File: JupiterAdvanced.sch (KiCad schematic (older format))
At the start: 217 parts, among them SW1 SW_Push, U1 PRTR5V0U2X, U2 AT90USB1286-AU, Y1 16MHz

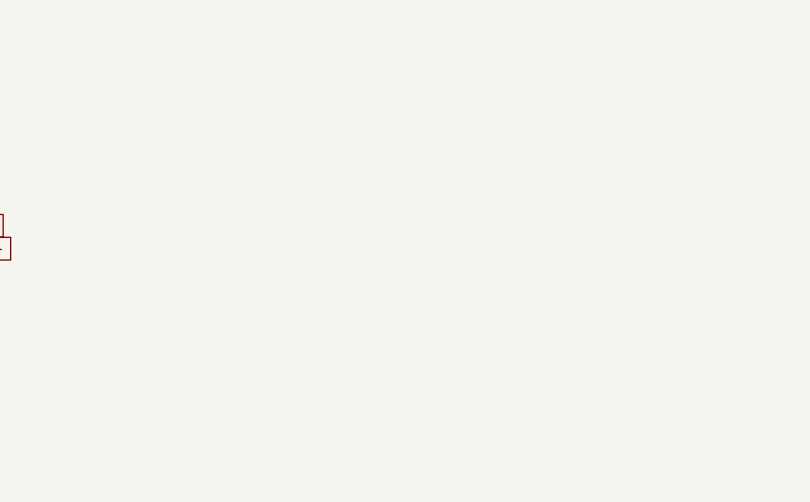
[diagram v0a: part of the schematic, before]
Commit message: Gerber Files updated, Drill holes added
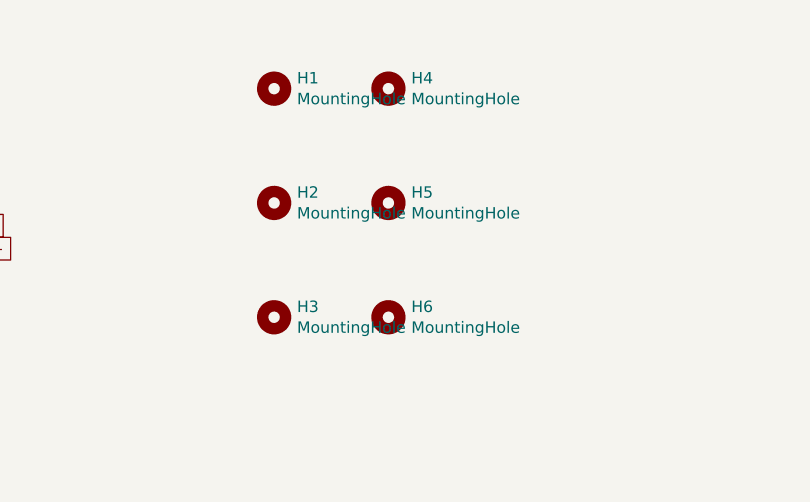
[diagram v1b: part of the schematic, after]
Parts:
- added H1, H2, H3, H4, H5, H6: MountingHole, MountingHole:MountingHole_2.5mm, symbol Mechanical:MountingHole
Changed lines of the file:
@@
 NoConn ~ 11050 4250
 NoConn ~ 11050 2350
+$Comp
+L Mechanical:MountingHole H4
+U 1 1 607B1DF0
+P 5900 1000
+F 0 "H4" H 6000 1046 50  0000 L CNN
+F 1 "MountingHole" H 6000 955 50  0000 L CNN
+F 2 "MountingHole:MountingHole_2.5mm" H 5900 1000 50  0001 C CNN
+F 3 "~" H 5900 1000 50  0001 C CNN
+	1    5900 1000
+	1    0    0    -1
+$EndComp
+$Comp
+L Mechanical:MountingHole H5
+U 1 1 607B3E5A
+P 5900 1500
+F 0 "H5" H 6000 1546 50  0000 L CNN
+F 1 "MountingHole" H 6000 1455 50  0000 L CNN
+F 2 "MountingHole:MountingHole_2.5mm" H 5900 1500 50  0001 C CNN
+F 3 "~" H 5900 1500 50  0001 C CNN
+	1    5900 1500
+	1    0    0    -1
+$EndComp
+$Comp
+L Mechanical:MountingHole H6
+U 1 1 607B462B
+P 5900 2000
+F 0 "H6" H 6000 2046 50  0000 L CNN
+F 1 "MountingHole" H 6000 1955 50  0000 L CNN
+F 2 "MountingHole:MountingHole_2.5mm" H 5900 2000 50  0001 C CNN
+F 3 "~" H 5900 2000 50  0001 C CNN
+	1    5900 2000
+	1    0    0    -1
+$EndComp
+$Comp
+L Mechanical:MountingHole H1
+U 1 1 607B5D34
+P 5400 1000
+F 0 "H1" H 5500 1046 50  0000 L CNN
+F 1 "MountingHole" H 5500 955 50  0000 L CNN
+F 2 "MountingHole:MountingHole_2.5mm" H 5400 1000 50  0001 C CNN
+F 3 "~" H 5400 1000 50  0001 C CNN
+	1    5400 1000
+	1    0    0    -1
+$EndComp
+$Comp
+L Mechanical:MountingHole H2
+U 1 1 607B60CD
+P 5400 1500
+F 0 "H2" H 5500 1546 50  0000 L CNN
+F 1 "MountingHole" H 5500 1455 50  0000 L CNN
+F 2 "MountingHole:MountingHole_2.5mm" H 5400 1500 50  0001 C CNN
+F 3 "~" H 5400 1500 50  0001 C CNN
+	1    5400 1500
+	1    0    0    -1
+$EndComp
+$Comp
+L Mechanical:MountingHole H3
+U 1 1 607B643D
+P 5400 2000
+F 0 "H3" H 5500 2046 50  0000 L CNN
+F 1 "MountingHole" H 5500 1955 50  0000 L CNN
+F 2 "MountingHole:MountingHole_2.5mm" H 5400 2000 50  0001 C CNN
+F 3 "~" H 5400 2000 50  0001 C CNN
+	1    5400 2000
+	1    0    0    -1
+$EndComp
 $EndSCHEMATC

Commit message: LCSC added to USB system
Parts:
- F11: LCSC (none) -> C163133
- R1, R3: LCSC (none) -> C27834
- U1: LCSC (none) -> C558444
- USB1: LCSC (none) -> C165948
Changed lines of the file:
@@
 F 2 "Type-C:HRO-TYPE-C-31-M-12-Assembly" H 1350 1550 60  0001 C CNN
 F 3 "" H 1350 1550 60  0001 C CNN
+F 4 "C165948" H 1350 1550 50  0001 C CNN "LCSC"
 	1    1350 1550
 	1    0    0    -1
@@
 F 2 "Fuse:Fuse_1206_3216Metric" H 2600 900 50  0001 L CNN
 F 3 "~" H 2550 1100 50  0001 C CNN
+F 4 "C163133" V 2550 1100 50  0001 C CNN "LCSC"
 	1    2550 1100
 	0    1    1    0
@@
 F 2 "Resistor_SMD:R_0805_2012Metric" H 2050 2350 50  0001 C CNN
 F 3 "~" H 2050 2350 50  0001 C CNN
+F 4 "C27834" H 2050 2350 50  0001 C CNN "LCSC"
 	1    2050 2350
 	1    0    0    -1
@@
 F 2 "Resistor_SMD:R_0805_2012Metric" H 2400 2350 50  0001 C CNN
 F 3 "~" H 2400 2350 50  0001 C CNN
+F 4 "C27834" H 2400 2350 50  0001 C CNN "LCSC"
 	1    2400 2350
 	1    0    0    -1
@@
 F 2 "random-keyboard-parts:SOT143B" H 3200 2400 60  0001 C CNN
 F 3 "" H 3200 2400 60  0001 C CNN
+F 4 "C558444 " H 3200 2400 50  0001 C CNN "LCSC"
 	1    3200 2400
 	-1   0    0    1

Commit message: LCSC parts numbers added
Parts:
- C1, C2, C3: LCSC (none) -> C1711
- C4: LCSC (none) -> C15850
- C5, C6: LCSC (none) -> C1804
- C7: LCSC (none) -> C28323
- R5, R6: LCSC (none) -> C17561
- R7, R8: LCSC (none) -> C17414
- Y1: LCSC (none) -> C89379
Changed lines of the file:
@@
 F 2 "Resistor_SMD:R_0805_2012Metric" H 10500 3750 50  0001 C CNN
 F 3 "~" H 10500 3750 50  0001 C CNN
+F 4 "C17414" V 10500 3750 50  0001 C CNN "LCSC"
 	1    10500 3750
 	0    1    1    0
@@
 F 2 "Capacitor_SMD:C_0805_2012Metric" H 10150 3150 50  0001 C CNN
 F 3 "~" H 10150 3150 50  0001 C CNN
+F 4 "C28323" H 10150 3150 50  0001 C CNN "LCSC"
 	1    10150 3150
 	-1   0    0    1
@@
 F 2 "Capacitor_SMD:C_0805_2012Metric" H 9400 1350 50  0001 C CNN
 F 3 "~" H 9400 1350 50  0001 C CNN
+F 4 "C1711" H 9400 1350 50  0001 C CNN "LCSC"
 	1    9400 1350
 	1    0    0    -1
@@
 F 2 "Capacitor_SMD:C_0805_2012Metric" H 9800 1350 50  0001 C CNN
 F 3 "~" H 9800 1350 50  0001 C CNN
+F 4 "C15850" H 9800 1350 50  0001 C CNN "LCSC"
 	1    9800 1350
 	1    0    0    -1
@@
 F 2 "Capacitor_SMD:C_0805_2012Metric" H 9000 1350 50  0001 C CNN
 F 3 "~" H 9000 1350 50  0001 C CNN
+F 4 "C1711" H 9000 1350 50  0001 C CNN "LCSC"
 	1    9000 1350
 	1    0    0    -1
@@
 F 2 "Capacitor_SMD:C_0805_2012Metric" H 8600 1350 50  0001 C CNN
 F 3 "~" H 8600 1350 50  0001 C CNN
+F 4 "C1711" H 8600 1350 50  0001 C CNN "LCSC"
 	1    8600 1350
 	1    0    0    -1
@@
 F 2 "Crystal:Crystal_SMD_3225-4Pin_3.2x2.5mm" H 10300 2050 50  0001 C CNN
 F 3 "~" H 10300 2050 50  0001 C CNN
+F 4 "C89379" V 10300 2050 50  0001 C CNN "LCSC"
 	1    10300 2050
 	0    1    1    0
@@
 F 2 "Capacitor_SMD:C_0805_2012Metric" H 9900 1850 50  0001 C CNN
 F 3 "~" H 9900 1850 50  0001 C CNN
+F 4 "C1804" V 9900 1850 50  0001 C CNN "LCSC"
 	1    9900 1850
 	0    1    1    0
@@
 F 2 "Capacitor_SMD:C_0805_2012Metric" H 9900 2200 50  0001 C CNN
 F 3 "~" H 9900 2200 50  0001 C CNN
+F 4 "C1804" V 9900 2200 50  0001 C CNN "LCSC"
 	1    9900 2200
 	0    1    1    0
@@
 F 2 "Resistor_SMD:R_0805_2012Metric" H 11000 1200 50  0001 C CNN
 F 3 "~" H 11000 1200 50  0001 C CNN
+F 4 "C17414" H 11000 1200 50  0001 C CNN "LCSC"
 	1    11000 1200
 	1    0    0    -1
@@
 F 2 "Resistor_SMD:R_0805_2012Metric" H 10200 2750 50  0001 C CNN
 F 3 "~" H 10200 2750 50  0001 C CNN
+F 4 "C17561" V 10200 2750 50  0001 C CNN "LCSC"
 	1    10200 2750
 	0    1    1    0
@@
 F 2 "Resistor_SMD:R_0805_2012Metric" H 10500 2850 50  0001 C CNN
 F 3 "~" H 10500 2850 50  0001 C CNN
+F 4 "C17561" V 10500 2850 50  0001 C CNN "LCSC"
 	1    10500 2850
 	0    1    1    0

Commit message: LCSC parts numbers added
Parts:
- D1, D10, D100, D11, D12, D13, D14, D15, D16, D17, D18, D19, D2, D20, D21, D22, D23, D24, D25, D26, D27, D28, D29, D3, D30, D32, D33, D34, D35, D36, D37, D38, D39, D4, D40, D41, D42, D43, D44, D45, D46, D47, D48, D49, D5, D50, D51, D52, D53, D54, D55, D56, D58, D59, D6, D60, D61, D62, D63, D64, D65, D66, D67, D68, D69, D7, D70, D71, D72, D73, D74, D75, D76, D77, D78, D79, D8, D80, D81, D82, D83, D84, D85, D86, D87, D88, D89, D9, D90, D91, D92, D93, D94, D95, D96, D97, D98, D99: LCSC (none) -> C81598
- D57: LSCS (none) -> C81598

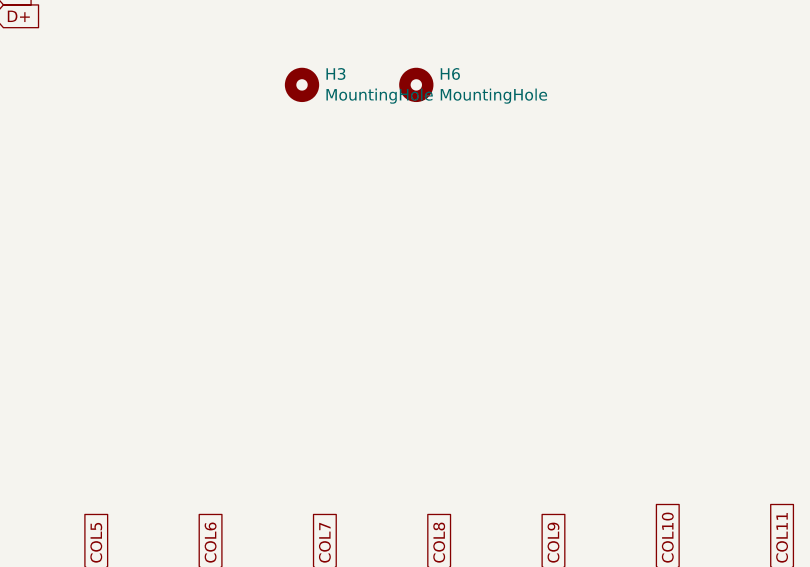
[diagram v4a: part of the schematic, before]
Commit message: Ferret Bead added on USB Ground
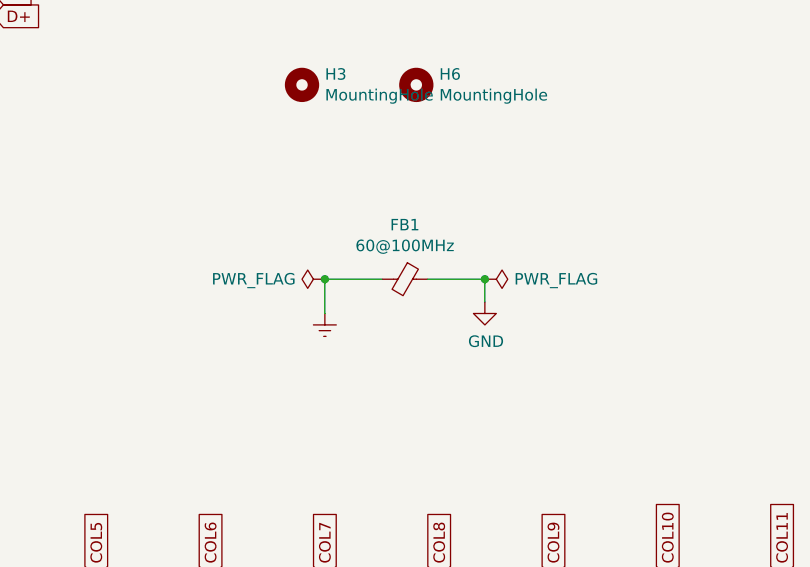
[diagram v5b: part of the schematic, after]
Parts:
- added FB1: 60@100MHz, Inductor_SMD:L_0805_2012Metric, symbol Device:Ferrite_Bead_Small
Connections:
- net labels added: Earth
- wire segments 405 -> 409
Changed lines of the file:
@@
 	1    0    0    -1
 $EndComp
+$Comp
+L Device:Ferrite_Bead_Small FB1
+U 1 1 607F6A7A
+P 5850 2850
+F 0 "FB1" V 5613 2850 50  0000 C CNN
+F 1 "60@100MHz" V 5704 2850 50  0000 C CNN
+F 2 "Inductor_SMD:L_0805_2012Metric" V 5780 2850 50  0001 C CNN
+F 3 "~" H 5850 2850 50  0001 C CNN
+	1    5850 2850
+	0    1    1    0
+$EndComp
+$Comp
+L power:GND #PWR0115
+U 1 1 607F9CFC
+P 6200 2950
+F 0 "#PWR0115" H 6200 2700 50  0001 C CNN
+F 1 "GND" H 6205 2777 50  0000 C CNN
+F 2 "" H 6200 2950 50  0001 C CNN
+F 3 "" H 6200 2950 50  0001 C CNN
+	1    6200 2950
+	1    0    0    -1
+$EndComp
+$Comp
+L power:Earth #PWR0116
+U 1 1 607FD133
+P 5500 3000
+F 0 "#PWR0116" H 5500 2750 50  0001 C CNN
+F 1 "Earth" H 5500 2850 50  0001 C CNN
+F 2 "" H 5500 3000 50  0001 C CNN
+F 3 "~" H 5500 3000 50  0001 C CNN
+	1    5500 3000
+	1    0    0    -1
+$EndComp
+Wire Wire Line
+	6200 2950 6200 2850
+Wire Wire Line
+	6200 2850 5950 2850
+Wire Wire Line
+	5750 2850 5500 2850
+Wire Wire Line
+	5500 2850 5500 3000
+$Comp
+L power:PWR_FLAG #FLG0104
+U 1 1 6086389D
+P 6200 2850
+F 0 "#FLG0104" H 6200 2925 50  0001 C CNN
+F 1 "PWR_FLAG" V 6200 2978 50  0000 L CNN
+F 2 "" H 6200 2850 50  0001 C CNN
+F 3 "~" H 6200 2850 50  0001 C CNN
+	1    6200 2850
+	0    1    1    0
+$EndComp
+Connection ~ 6200 2850
+$Comp
+L power:PWR_FLAG #FLG0105
+U 1 1 60866D1D
+P 5500 2850
+F 0 "#FLG0105" H 5500 2925 50  0001 C CNN
+F 1 "PWR_FLAG" V 5500 2977 50  0000 L CNN
+F 2 "" H 5500 2850 50  0001 C CNN
+F 3 "~" H 5500 2850 50  0001 C CNN
+	1    5500 2850
+	0    -1   -1   0
+$EndComp
+Connection ~ 5500 2850
 $EndSCHEMATC

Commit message: Mounting holes updated
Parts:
- H1, H2, H3, H4, H5, H6: footprint MountingHole:MountingHole_2.5mm -> MountingHole:MountingHole_2.5mm_Pad
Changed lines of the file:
@@
 F 0 "H4" H 6000 1046 50  0000 L CNN
 F 1 "MountingHole" H 6000 955 50  0000 L CNN
-F 2 "MountingHole:MountingHole_2.5mm" H 5900 1000 50  0001 C CNN
+F 2 "MountingHole:MountingHole_2.5mm_Pad" H 5900 1000 50  0001 C CNN
 F 3 "~" H 5900 1000 50  0001 C CNN
 	1    5900 1000
@@
 F 0 "H5" H 6000 1546 50  0000 L CNN
 F 1 "MountingHole" H 6000 1455 50  0000 L CNN
-F 2 "MountingHole:MountingHole_2.5mm" H 5900 1500 50  0001 C CNN
+F 2 "MountingHole:MountingHole_2.5mm_Pad" H 5900 1500 50  0001 C CNN
 F 3 "~" H 5900 1500 50  0001 C CNN
 	1    5900 1500
@@
 F 0 "H6" H 6000 2046 50  0000 L CNN
 F 1 "MountingHole" H 6000 1955 50  0000 L CNN
-F 2 "MountingHole:MountingHole_2.5mm" H 5900 2000 50  0001 C CNN
+F 2 "MountingHole:MountingHole_2.5mm_Pad" H 5900 2000 50  0001 C CNN
 F 3 "~" H 5900 2000 50  0001 C CNN
 	1    5900 2000
@@
 F 0 "H1" H 5500 1046 50  0000 L CNN
 F 1 "MountingHole" H 5500 955 50  0000 L CNN
-F 2 "MountingHole:MountingHole_2.5mm" H 5400 1000 50  0001 C CNN
+F 2 "MountingHole:MountingHole_2.5mm_Pad" H 5400 1000 50  0001 C CNN
 F 3 "~" H 5400 1000 50  0001 C CNN
 	1    5400 1000
@@
 F 0 "H2" H 5500 1546 50  0000 L CNN
 F 1 "MountingHole" H 5500 1455 50  0000 L CNN
-F 2 "MountingHole:MountingHole_2.5mm" H 5400 1500 50  0001 C CNN
+F 2 "MountingHole:MountingHole_2.5mm_Pad" H 5400 1500 50  0001 C CNN
 F 3 "~" H 5400 1500 50  0001 C CNN
 	1    5400 1500
@@
 F 0 "H3" H 5500 2046 50  0000 L CNN
 F 1 "MountingHole" H 5500 1955 50  0000 L CNN
-F 2 "MountingHole:MountingHole_2.5mm" H 5400 2000 50  0001 C CNN
+F 2 "MountingHole:MountingHole_2.5mm_Pad" H 5400 2000 50  0001 C CNN
 F 3 "~" H 5400 2000 50  0001 C CNN
 	1    5400 2000

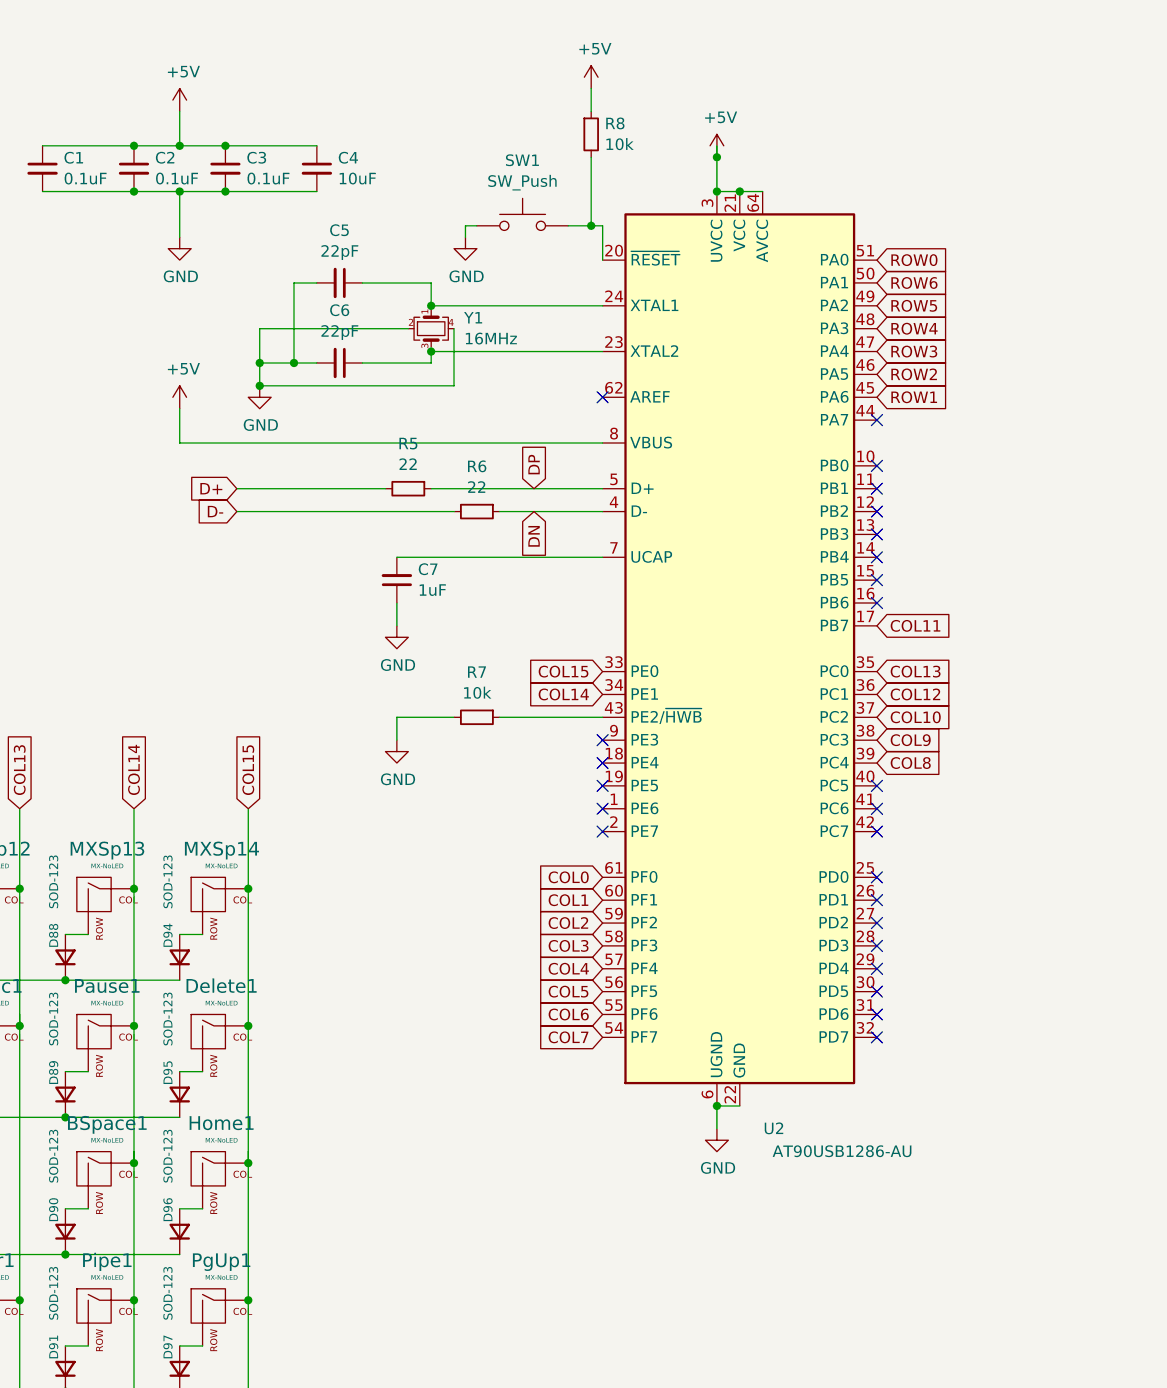
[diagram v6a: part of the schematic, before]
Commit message: ATMega32u4 MCU added
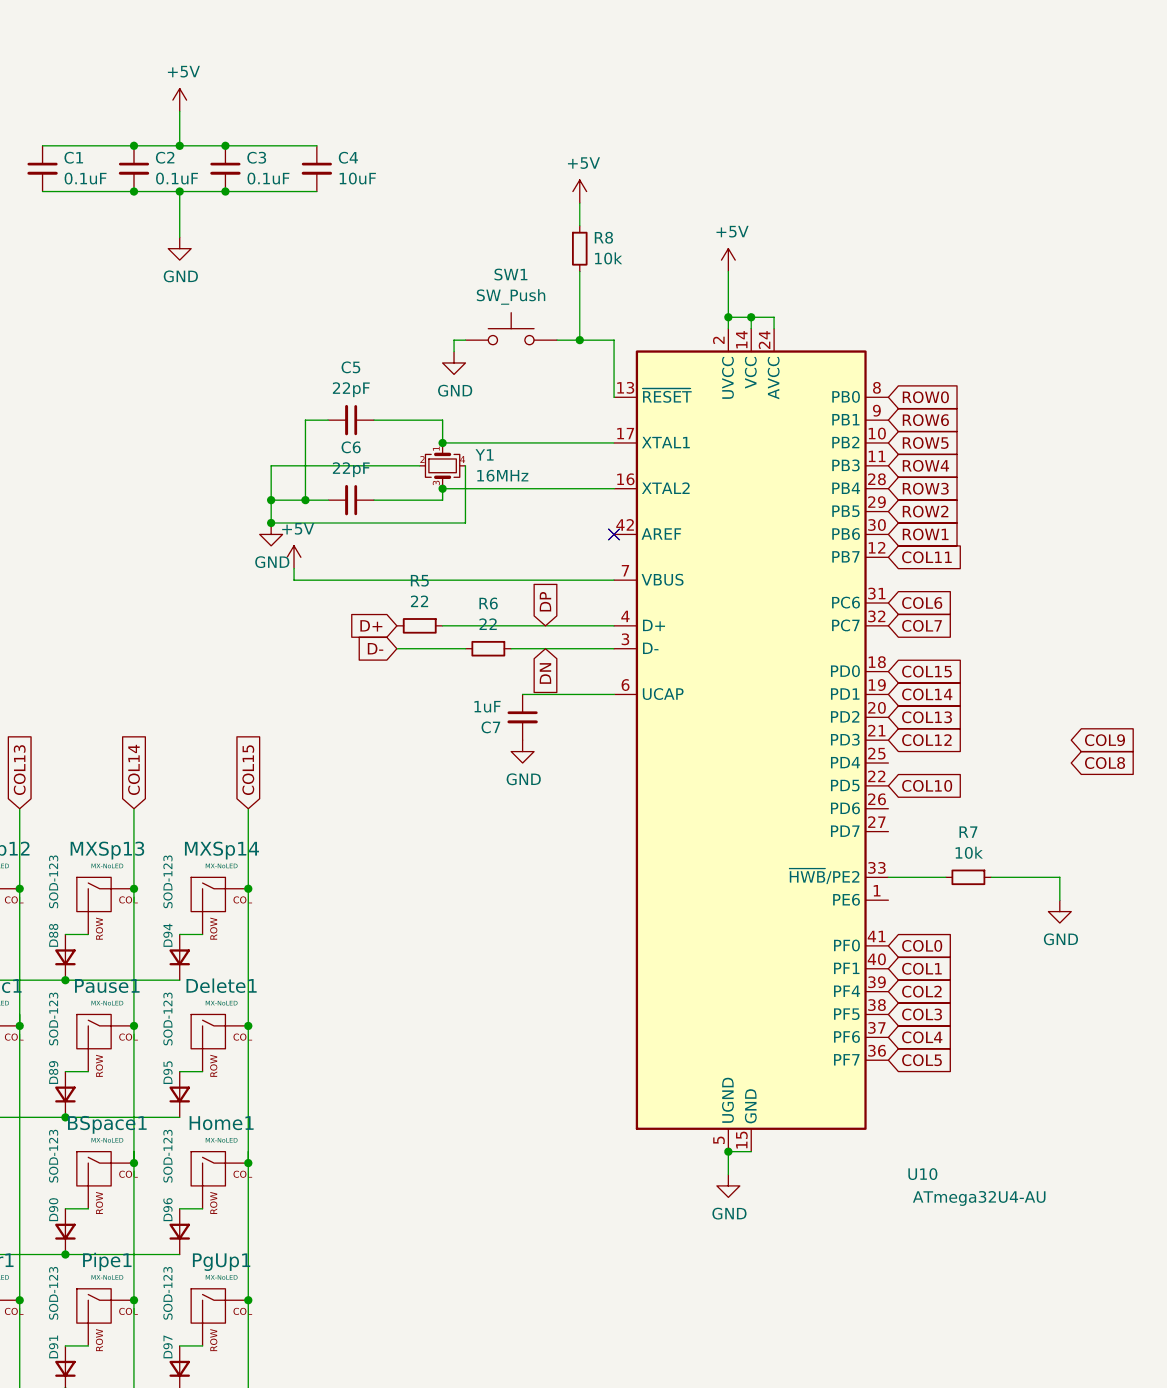
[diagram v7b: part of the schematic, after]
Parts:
- removed U2: AT90USB1286-AU, Package_QFP:TQFP-64_14x14mm_P0.8mm, symbol MCU_Microchip_AVR:AT90USB1286-AU
- added U10: ATmega32U4-AU, Package_QFP:TQFP-44_10x10mm_P0.8mm, symbol MCU_Microchip_ATmega:ATmega32U4-AU
- H1, H2, H3, H4, H5, H6: footprint MountingHole:MountingHole_2.5mm_Pad -> MountingHole:MountingHole_2.5mm
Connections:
- no-connect marks 27 -> 3
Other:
- moved on the sheet: C5, C6, C7, R5, R6, R7, R8, SW1, Y1
